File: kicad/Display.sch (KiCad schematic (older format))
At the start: 34 parts, among them P201 CONN_01X06, P202 CONN_01X07, P203 CONN_01X06, P204 CONN_01X07, Q201 BC856BS, Q202 BC856BS, Q203 BC856BS, U201 SN74LS138, U202 74HC4511

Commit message: Changes to the gerbers
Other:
- moved on the sheet: P201, P203
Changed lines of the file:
@@
 	9450 5150 9850 5150
 Wire Wire Line
-	9450 850  10150 850
+	9450 850  9900 850
+Wire Wire Line
+	9900 850  10150 850
 Wire Wire Line
 	9900 950  9900 850
@@
 	7250 2050 7750 2050
 Wire Wire Line
-	9450 2250 10150 2250
+	9450 2250 9850 2250
+Wire Wire Line
+	9850 2250 10150 2250
 Wire Wire Line
 	9450 950  9900 950
 Wire Wire Line
-	9450 3750 10150 3750
-Wire Wire Line
-	9450 5050 10150 5050
-Wire Bus Line
-	7850 1000 7850 5600
+	9450 3750 9850 3750
+Wire Wire Line
+	9850 3750 10150 3750
+Wire Wire Line
+	9450 5050 9850 5050
+Wire Wire Line
+	9850 5050 10150 5050
+Wire Bus Line
+	7850 1000 7850 1100
+Wire Bus Line
+	7850 1100 7850 1200
+Wire Bus Line
+	7850 1200 7850 1300
+Wire Bus Line
+	7850 1300 7850 1400
+Wire Bus Line
+	7850 1400 7850 1500
+Wire Bus Line
+	7850 1500 7850 1550
+Wire Bus Line
+	7850 1550 7850 1600
+Wire Bus Line
+	7850 1600 7850 1650
+Wire Bus Line
+	7850 1650 7850 1750
+Wire Bus Line
+	7850 1750 7850 1850
+Wire Bus Line
+	7850 1850 7850 1950
+Wire Bus Line
+	7850 1950 7850 2050
+Wire Bus Line
+	7850 2050 7850 2150
+Wire Bus Line
+	7850 2150 7850 2200
+Wire Bus Line
+	7850 2200 7850 2300
+Wire Bus Line
+	7850 2300 7850 2400
+Wire Bus Line
+	7850 2400 7850 2500
+Wire Bus Line
+	7850 2500 7850 2600
+Wire Bus Line
+	7850 2600 7850 2700
+Wire Bus Line
+	7850 2700 7850 2800
+Wire Bus Line
+	7850 2800 7850 3700
+Wire Bus Line
+	7850 3700 7850 3800
+Wire Bus Line
+	7850 3800 7850 3900
+Wire Bus Line
+	7850 3900 7850 4000
+Wire Bus Line
+	7850 4000 7850 4100
+Wire Bus Line
+	7850 4100 7850 4200
+Wire Bus Line
+	7850 4200 7850 4300
+Wire Bus Line
+	7850 4300 7850 5000
+Wire Bus Line
+	7850 5000 7850 5100
+Wire Bus Line
+	7850 5100 7850 5200
+Wire Bus Line
+	7850 5200 7850 5300
+Wire Bus Line
+	7850 5300 7850 5400
+Wire Bus Line
+	7850 5400 7850 5500
+Wire Bus Line
+	7850 5500 7850 5600
 $Comp
 L 74HC4511 U202
@@
 	2400 750  2700 750
 Wire Wire Line
-	2400 1950 3000 1950
-Wire Wire Line
-	2400 1050 2950 1050
+	2400 1950 2700 1950
+Wire Wire Line
+	2700 1950 3000 1950
+Wire Wire Line
+	2400 1050 2700 1050
+Wire Wire Line
+	2700 1050 2950 1050
 Connection ~ 2700 1050
 Wire Wire Line
@@
 L VCC #PWR015
 U 1 1 55871329
-P 1750 2500
-F 0 "#PWR015" H 1750 2350 50  0001 C CNN
-F 1 "VCC" H 1750 2650 50  0000 C CNN
-F 2 "" H 1750 2500 60  0000 C CNN
-F 3 "" H 1750 2500 60  0000 C CNN
-	1    1750 2500
-	1    0    0    -1
-$EndComp
-Wire Wire Line
-	1750 2500 1750 2650
+P 1750 2600
+F 0 "#PWR015" H 1750 2450 50  0001 C CNN
+F 1 "VCC" H 1750 2750 50  0000 C CNN
+F 2 "" H 1750 2600 60  0000 C CNN
+F 3 "" H 1750 2600 60  0000 C CNN
+	1    1750 2600
+	1    0    0    -1
+$EndComp
+Wire Wire Line
+	1750 2600 1750 2650
 $Comp
 L GND #PWR016
@@
 $EndComp
 Wire Wire Line
-	1750 4150 1750 4400
+	1750 4150 1750 4300
+Wire Wire Line
+	1750 4300 1750 4400
 Wire Wire Line
 	1150 3650 950  3650
 Wire Wire Line
-	950  3650 950  4300
+	950  3650 950  3750
+Wire Wire Line
+	950  3750 950  4300
 Wire Wire Line
 	950  4300 1750 4300
@@
 $EndComp
 Wire Wire Line
-	1850 6350 2450 6350
+	1850 6350 2200 6350
+Wire Wire Line
+	2200 6350 2450 6350
 Wire Wire Line
 	2450 6450 2200 6450
@@
 $EndComp
 Wire Wire Line
-	3000 7000 3000 7150
+	3000 7000 3000 7100
+Wire Wire Line
+	3000 7100 3000 7150
 Wire Wire Line
 	2450 6550 2300 6550
@@
 L CONN_01X06 P201
 U 1 1 5589B385
-P 5000 1650
-F 0 "P201" H 5000 2000 50  0000 C CNN
-F 1 "CONN_01X06" V 5100 1650 50  0000 C CNN
-F 2 "Pin_Headers:Pin_Header_Straight_1x06" H 5000 1650 60  0001 C CNN
-F 3 "" H 5000 1650 60  0000 C CNN
-	1    5000 1650
+P 4950 1000
+F 0 "P201" H 4950 1350 50  0000 C CNN
+F 1 "CONN_01X06" V 5050 1000 50  0000 C CNN
+F 2 "Pin_Headers:Pin_Header_Straight_1x06" H 4950 1000 60  0001 C CNN
+F 3 "" H 4950 1000 60  0000 C CNN
+	1    4950 1000
 	-1   0    0    -1
 $EndComp
-Text GLabel 5450 1400 2    60   Input ~ 0
+Text GLabel 5400 750  2    60   Input ~ 0
 D_Dig_0
-Text GLabel 5450 1500 2    60   Input ~ 0
+Text GLabel 5400 850  2    60   Input ~ 0
 D_Dig_1
-Text GLabel 5450 1600 2    60   Input ~ 0
+Text GLabel 5400 950  2    60   Input ~ 0
 D_Dig_2
-Text GLabel 5450 1700 2    60   Input ~ 0
+Text GLabel 5400 1050 2    60   Input ~ 0
 D_Dig_3
-Text GLabel 5450 1900 2    60   Input ~ 0
+Text GLabel 5400 1250 2    60   Input ~ 0
 D_Signal
-Text GLabel 5450 1800 2    60   Input ~ 0
+Text GLabel 5400 1150 2    60   Input ~ 0
 D_Colon
 Wire Wire Line
-	5200 1400 5450 1400
-Wire Wire Line
-	5450 1500 5200 1500
-Wire Wire Line
-	5200 1600 5450 1600
-Wire Wire Line
-	5450 1700 5200 1700
-Wire Wire Line
-	5200 1800 5450 1800
-Wire Wire Line
-	5450 1900 5200 1900
+	5150 750  5400 750
+Wire Wire Line
+	5400 850  5150 850
+Wire Wire Line
+	5150 950  5400 950
+Wire Wire Line
+	5400 1050 5150 1050
+Wire Wire Line
+	5150 1150 5400 1150
+Wire Wire Line
+	5400 1250 5150 1250
 $Comp
 L CONN_01X07 P204
@@
 L CONN_01X06 P203
 U 1 1 5589E43E
-P 6350 2750
-F 0 "P203" H 6350 3100 50  0000 C CNN
-F 1 "CONN_01X06" V 6450 2750 50  0000 C CNN
-F 2 "Pin_Headers:Pin_Header_Straight_1x06" H 6350 2750 60  0001 C CNN
-F 3 "" H 6350 2750 60  0000 C CNN
-	1    6350 2750
-	1    0    0    -1
-$EndComp
-Text GLabel 5900 2500 0    60   Input ~ 0
+P 5800 1850
+F 0 "P203" H 5800 2200 50  0000 C CNN
+F 1 "CONN_01X06" V 5900 1850 50  0000 C CNN
+F 2 "Pin_Headers:Pin_Header_Straight_1x06" H 5800 1850 60  0001 C CNN
+F 3 "" H 5800 1850 60  0000 C CNN
+	1    5800 1850
+	1    0    0    -1
+$EndComp
+Text GLabel 5350 1600 0    60   Input ~ 0
 C_Dig_0
-Text GLabel 5900 2600 0    60   Input ~ 0
+Text GLabel 5350 1700 0    60   Input ~ 0
 C_Dig_1
-Text GLabel 5900 2700 0    60   Input ~ 0
+Text GLabel 5350 1800 0    60   Input ~ 0
 C_Dig_2
-Text GLabel 5900 2800 0    60   Input ~ 0
+Text GLabel 5350 1900 0    60   Input ~ 0
 C_Dig_3
-Text GLabel 5900 2900 0    60   Input ~ 0
+Text GLabel 5350 2000 0    60   Input ~ 0
 C_Colon
-Text GLabel 5900 3000 0    60   Input ~ 0
+Text GLabel 5350 2100 0    60   Input ~ 0
 C_Signal
 Wire Wire Line
-	5900 2500 6150 2500
-Wire Wire Line
-	6150 2600 5900 2600
-Wire Wire Line
-	5900 2700 6150 2700
-Wire Wire Line
-	6150 2800 5900 2800
-Wire Wire Line
-	5900 2900 6150 2900
-Wire Wire Line
-	6150 3000 5900 3000
+	5350 1600 5600 1600
+Wire Wire Line
+	5600 1700 5350 1700
+Wire Wire Line
+	5350 1800 5600 1800
+Wire Wire Line
+	5600 1900 5350 1900
+Wire Wire Line
+	5350 2000 5600 2000
+Wire Wire Line
+	5600 2100 5350 2100
 $Comp
 L BC856BS Q201

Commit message: small correction
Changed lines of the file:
@@
 	9450 5150 9850 5150
 Wire Wire Line
-	9450 850  9900 850
-Wire Wire Line
-	9900 850  10150 850
+	9450 850  10150 850
 Wire Wire Line
 	9900 950  9900 850
@@
 	7250 2050 7750 2050
 Wire Wire Line
-	9450 2250 9850 2250
-Wire Wire Line
-	9850 2250 10150 2250
+	9450 2250 10150 2250
 Wire Wire Line
 	9450 950  9900 950
 Wire Wire Line
-	9450 3750 9850 3750
-Wire Wire Line
-	9850 3750 10150 3750
-Wire Wire Line
-	9450 5050 9850 5050
-Wire Wire Line
-	9850 5050 10150 5050
+	9450 3750 10150 3750
+Wire Wire Line
+	9450 5050 10150 5050
 Wire Bus Line
-	7850 1000 7850 1100
-Wire Bus Line
-	7850 1100 7850 1200
-Wire Bus Line
-	7850 1200 7850 1300
-Wire Bus Line
-	7850 1300 7850 1400
-Wire Bus Line
-	7850 1400 7850 1500
-Wire Bus Line
-	7850 1500 7850 1550
-Wire Bus Line
-	7850 1550 7850 1600
-Wire Bus Line
-	7850 1600 7850 1650
-Wire Bus Line
-	7850 1650 7850 1750
-Wire Bus Line
-	7850 1750 7850 1850
-Wire Bus Line
-	7850 1850 7850 1950
-Wire Bus Line
-	7850 1950 7850 2050
-Wire Bus Line
-	7850 2050 7850 2150
-Wire Bus Line
-	7850 2150 7850 2200
-Wire Bus Line
-	7850 2200 7850 2300
-Wire Bus Line
-	7850 2300 7850 2400
-Wire Bus Line
-	7850 2400 7850 2500
-Wire Bus Line
-	7850 2500 7850 2600
-Wire Bus Line
-	7850 2600 7850 2700
-Wire Bus Line
-	7850 2700 7850 2800
-Wire Bus Line
-	7850 2800 7850 3700
-Wire Bus Line
-	7850 3700 7850 3800
-Wire Bus Line
-	7850 3800 7850 3900
-Wire Bus Line
-	7850 3900 7850 4000
-Wire Bus Line
-	7850 4000 7850 4100
-Wire Bus Line
-	7850 4100 7850 4200
-Wire Bus Line
-	7850 4200 7850 4300
-Wire Bus Line
-	7850 4300 7850 5000
-Wire Bus Line
-	7850 5000 7850 5100
-Wire Bus Line
-	7850 5100 7850 5200
-Wire Bus Line
-	7850 5200 7850 5300
-Wire Bus Line
-	7850 5300 7850 5400
-Wire Bus Line
-	7850 5400 7850 5500
-Wire Bus Line
-	7850 5500 7850 5600
+	7850 1000 7850 5600
 $Comp
 L 74HC4511 U202
@@
 	2400 750  2700 750
 Wire Wire Line
-	2400 1950 2700 1950
-Wire Wire Line
-	2700 1950 3000 1950
-Wire Wire Line
-	2400 1050 2700 1050
-Wire Wire Line
-	2700 1050 2950 1050
+	2400 1950 3000 1950
+Wire Wire Line
+	2400 1050 2950 1050
 Connection ~ 2700 1050
 Wire Wire Line
@@
 U 1 1 5587356B
 P 3900 5750
-F 0 "R211" V 3980 5750 50  0000 C CNN
+F 0 "R211" V 3850 5550 50  0000 C CNN
 F 1 "160" V 3900 5750 50  0000 C CNN
 F 2 "Resistors_SMD:R_0805_HandSoldering" V 3830 5750 30  0001 C CNN
@@
 U 1 1 55873774
 P 3900 5850
-F 0 "R212" V 3980 5850 50  0000 C CNN
+F 0 "R212" V 3850 5650 50  0000 C CNN
 F 1 "160" V 3900 5850 50  0000 C CNN
 F 2 "Resistors_SMD:R_0805_HandSoldering" V 3830 5850 30  0001 C CNN
@@
 U 1 1 5587381A
 P 3900 5950
-F 0 "R213" V 3980 5950 50  0000 C CNN
+F 0 "R213" V 3850 5750 50  0000 C CNN
 F 1 "160" V 3900 5950 50  0000 C CNN
 F 2 "Resistors_SMD:R_0805_HandSoldering" V 3830 5950 30  0001 C CNN
@@
 U 1 1 55873877
 P 3900 6050
-F 0 "R214" V 3980 6050 50  0000 C CNN
+F 0 "R214" V 3850 5850 50  0000 C CNN
 F 1 "160" V 3900 6050 50  0000 C CNN
 F 2 "Resistors_SMD:R_0805_HandSoldering" V 3830 6050 30  0001 C CNN
@@
 U 1 1 55873973
 P 3900 6150
-F 0 "R215" V 3980 6150 50  0000 C CNN
+F 0 "R215" V 3850 5950 50  0000 C CNN
 F 1 "160" V 3900 6150 50  0000 C CNN
 F 2 "Resistors_SMD:R_0805_HandSoldering" V 3830 6150 30  0001 C CNN
@@
 U 1 1 558739F1
 P 3900 6250
-F 0 "R216" V 3980 6250 50  0000 C CNN
+F 0 "R216" V 3850 6050 50  0000 C CNN
 F 1 "160" V 3900 6250 50  0000 C CNN
 F 2 "Resistors_SMD:R_0805_HandSoldering" V 3830 6250 30  0001 C CNN
@@
 U 1 1 55873A73
 P 3900 6350
-F 0 "R217" V 3980 6350 50  0000 C CNN
+F 0 "R217" V 3850 6150 50  0000 C CNN
 F 1 "160" V 3900 6350 50  0000 C CNN
 F 2 "Resistors_SMD:R_0805_HandSoldering" V 3830 6350 30  0001 C CNN
@@
 $EndComp
 Wire Wire Line
-	1750 4150 1750 4300
-Wire Wire Line
-	1750 4300 1750 4400
+	1750 4150 1750 4400
 Wire Wire Line
 	1150 3650 950  3650
 Wire Wire Line
-	950  3650 950  3750
-Wire Wire Line
-	950  3750 950  4300
+	950  3650 950  4300
 Wire Wire Line
 	950  4300 1750 4300
@@
 $EndComp
 Wire Wire Line
-	1850 6350 2200 6350
-Wire Wire Line
-	2200 6350 2450 6350
+	1850 6350 2450 6350
 Wire Wire Line
 	2450 6450 2200 6450
@@
 $EndComp
 Wire Wire Line
-	3000 7000 3000 7100
-Wire Wire Line
-	3000 7100 3000 7150
+	3000 7000 3000 7150
 Wire Wire Line
 	2450 6550 2300 6550
@@
 	1    0    0    -1
 $EndComp
-Text Label 4150 5750 0    60   ~ 0
+Text Label 4450 5750 0    60   ~ 0
 C_Seg_A
-Text Label 4150 5850 0    60   ~ 0
+Text Label 4450 5850 0    60   ~ 0
 C_Seg_B
-Text Label 4150 5950 0    60   ~ 0
+Text Label 4450 5950 0    60   ~ 0
 C_Seg_C
-Text Label 4150 6050 0    60   ~ 0
+Text Label 4450 6050 0    60   ~ 0
 C_Seg_D
-Text Label 4150 6150 0    60   ~ 0
+Text Label 4450 6150 0    60   ~ 0
 C_Seg_E
-Text Label 4150 6250 0    60   ~ 0
+Text Label 4450 6250 0    60   ~ 0
 C_Seg_F
-Text Label 4150 6350 0    60   ~ 0
+Text Label 4450 6350 0    60   ~ 0
 C_Seg_G
 Wire Wire Line

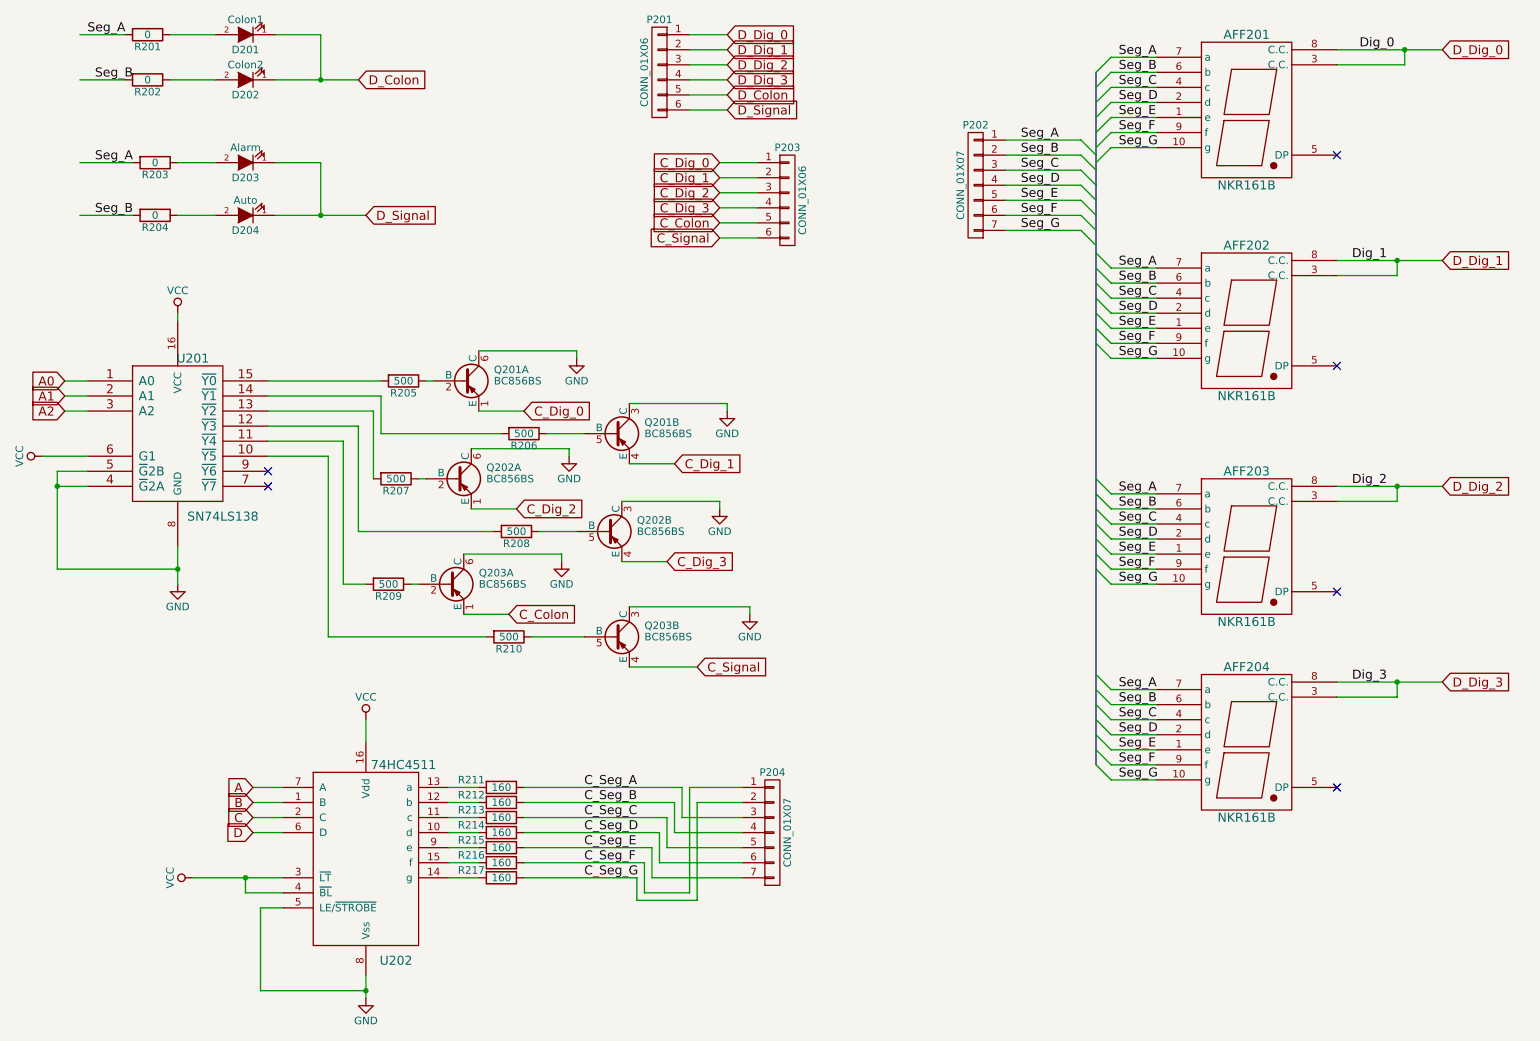
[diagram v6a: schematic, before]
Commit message: Updated main project with fixes from issues discovered when brining up the board
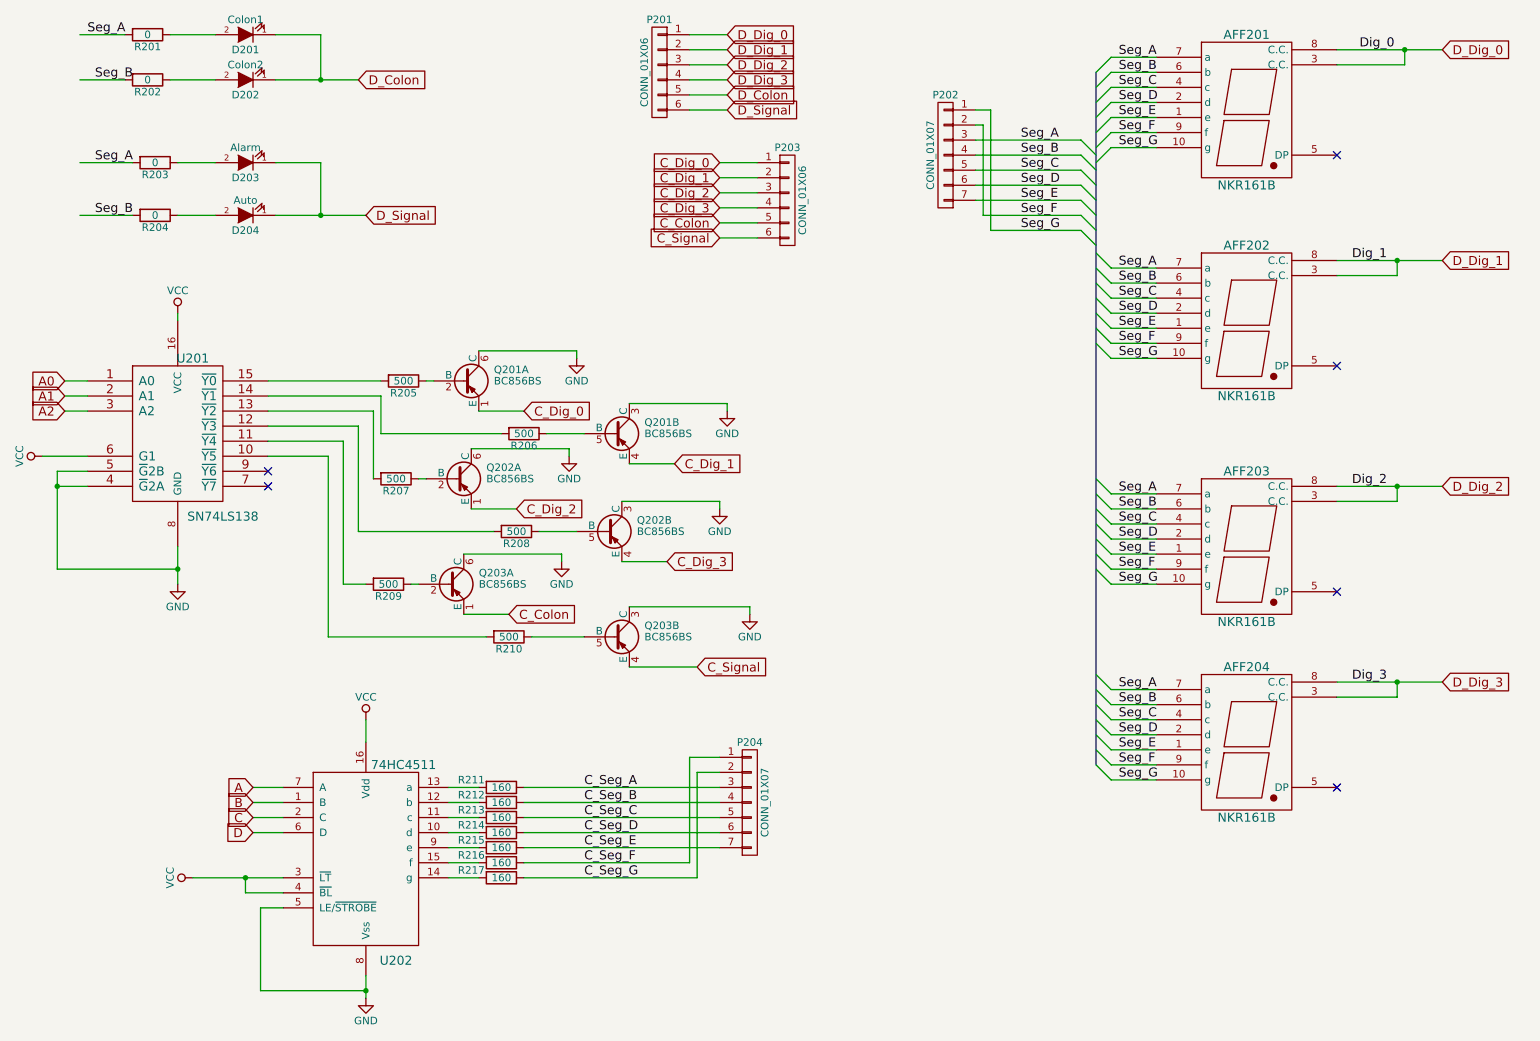
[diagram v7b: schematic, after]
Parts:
- R201, R202, R203, R204, R205, R206, R207, R208, R209, R210, R211, R212, R213, R214, R215, R216, R217: footprint Resistors_SMD:R_0805_HandSoldering -> Resistors_SMD:R_0805
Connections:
- net Seg_A: now also P202.3 (P3); no longer P202.1 (P1)
- net Seg_B: now also P202.4 (P4); no longer P202.2 (P2)
- net Seg_C: now also P202.5 (P5); no longer P202.3 (P3)
- net Seg_D: now also P202.6 (P6); no longer P202.4 (P4)
- net Seg_E: now also P202.7 (P7); no longer P202.5 (P5)
- net Seg_F: now also P202.2 (P2); no longer P202.6 (P6)
- net Seg_G: now also P202.1 (P1); no longer P202.7 (P7)
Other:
- moved on the sheet: P202, P204
